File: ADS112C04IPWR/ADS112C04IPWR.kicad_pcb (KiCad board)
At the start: 2 copper layers, 22.9 x 22.9 mm, 3 parts, among them J1 Conn_01x08, J2 Conn_01x08, U1 ADS112C04IPWR

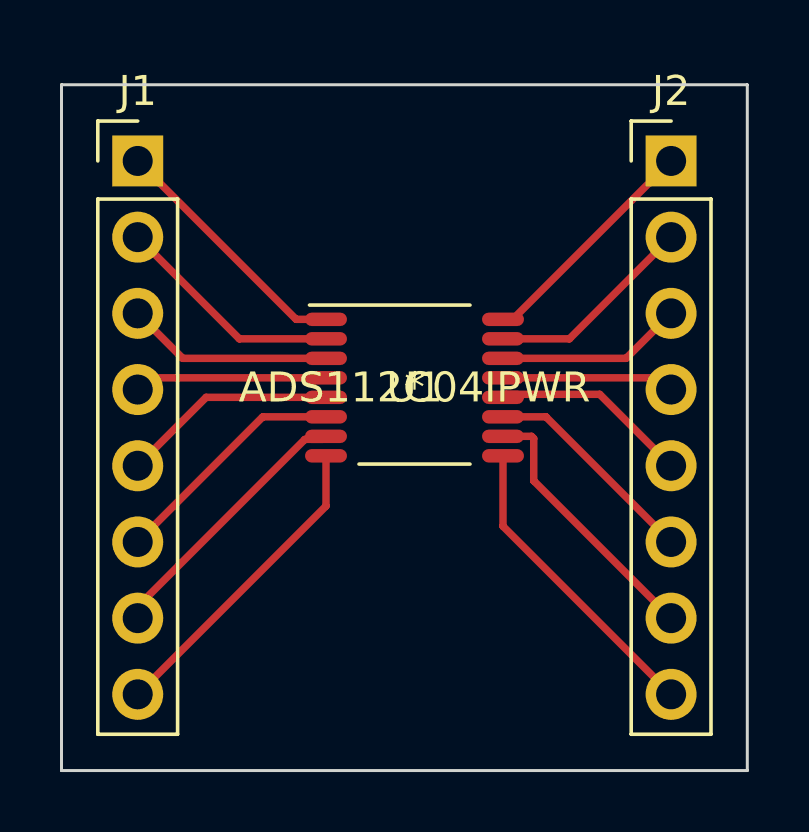
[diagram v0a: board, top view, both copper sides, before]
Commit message: Updating the ADC
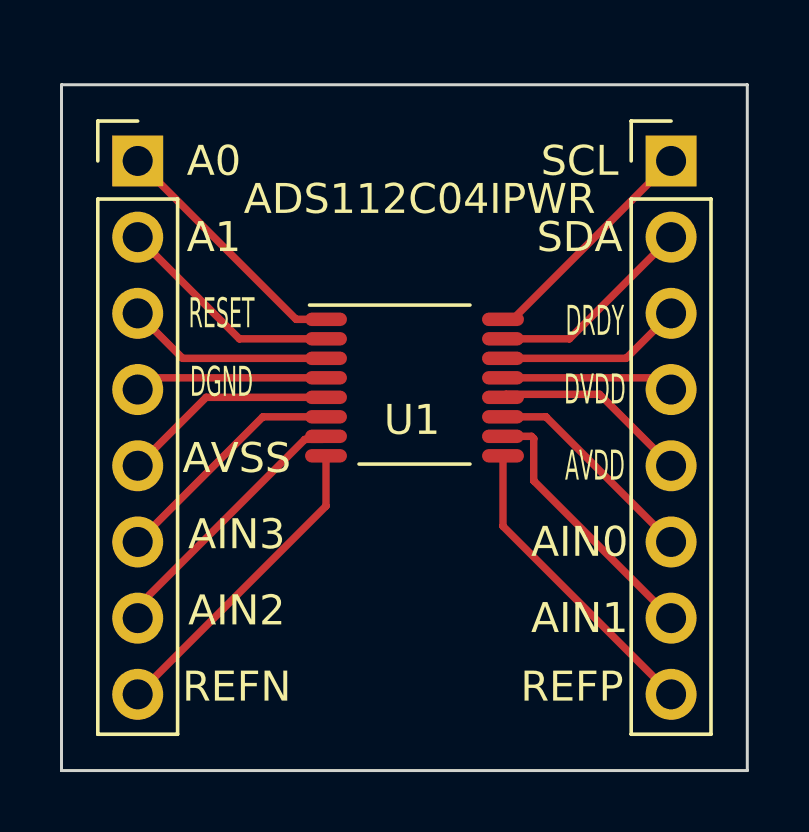
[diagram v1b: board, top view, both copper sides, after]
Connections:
- net Net-(J1-Pad4) renamed GNDD
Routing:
- added copper zone on B.Cu, net GNDD
- added copper zone on F.Cu, net GNDD
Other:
- board text added: "A0"
- board text added: "A1"
- board text added: "AIN0"
- board text added: "AIN1"
- board text added: "AIN2"
- board text added: "AIN3"
- board text added: "AVDD"
- board text added: "AVSS"
- board text added: "DGND"
- board text added: "DRDY"
- board text added: "DVDD"
- board text added: "REFN"
- board text added: "REFP"
- board text added: "RESET"
- board text added: "SCL"
- board text added: "SDA"
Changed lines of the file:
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@@
       (outputformat 1)
       (mirror false)
-      (drillshape 1)
+      (drillshape 0)
       (scaleselection 1)
       (outputdirectory "")
@@
   (net 2 "Net-(J1-Pad2)")
   (net 3 "Net-(J1-Pad3)")
-  (net 4 "Net-(J1-Pad4)")
+  (net 4 "GNDD")
   (net 5 "Net-(J1-Pad5)")
   (net 6 "Net-(J1-Pad6)")
@@
     (property "Sheetfile" "ADS112C04IPWR.kicad_sch")
     (property "Sheetname" "")
-    (attr through_hole)
-    (fp_text reference "U1" (at 0 0) (layer "F.SilkS")
-      (effects (font (size 1 1) (thickness 0.15)))
-    )
-    (fp_text value "ADS112C04IPWR" (at 0 0) (layer "F.SilkS")
-      (effects (font (size 1 1) (thickness 0.15)))
-    )
-    (fp_text user "*" (at 0 0) (layer "F.SilkS")
+    (attr smd)
+    (fp_text reference "U1" (at -0.0826 1.081795) (layer "F.SilkS")
+      (effects (font (size 1 1) (thickness 0.15)))
+    )
+    (fp_text value "ADS112C04IPWR" (at 0.1714 -6.284205) (layer "F.SilkS")
       (effects (font (size 1 1) (thickness 0.15)))
     )
@@
     (fp_line (start -3.9 2.799999) (end -3.9 -2.799999) (layer "F.CrtYd") (width 0.05))
     (fp_line (start 3.9 2.799999) (end 3.9 -2.799999) (layer "F.CrtYd") (width 0.05))
-    (fp_line (start -0.499999 0) (end 0.500002 0) (layer "F.CrtYd") (width 0.05))
     (fp_line (start -3.9 2.799999) (end 3.9 2.799999) (layer "F.CrtYd") (width 0.05))
-    (fp_line (start 0 0.500002) (end 0 -0.499999) (layer "F.CrtYd") (width 0.05))
     (fp_line (start -2.200001 -2.152503) (end -2.200001 -2.397486) (layer "F.Fab") (width 0.1))
     (fp_line (start -2.88669 1.747515) (end -2.739065 1.747515) (layer "F.Fab") (width 0.1))
@@
       (net 3 "Net-(J1-Pad3)") (pinfunction "RESET_N") (pintype "input"))
     (pad "4" smd oval (at -2.949999 -0.324998 90) (size 0.449999 1.4) (layers "F.Cu" "F.Paste" "F.Mask")
-      (net 4 "Net-(J1-Pad4)") (pinfunction "DGND") (pintype "power_in"))
+      (net 4 "GNDD") (pinfunction "DGND") (pintype "power_in"))
     (pad "5" smd oval (at -2.949999 0.325001 90) (size 0.449999 1.4) (layers "F.Cu" "F.Paste" "F.Mask")
       (net 5 "Net-(J1-Pad5)") (pinfunction "AVSS") (pintype "power_in"))
@@
     (property "Sheetname" "")
     (attr through_hole)
-    (fp_text reference "J2" (at 0 -2.33) (layer "F.SilkS")
+    (fp_text reference "J2" (at 0 -2.33) (layer "F.SilkS") hide
       (effects (font (size 1 1) (thickness 0.15)))
     )
@@
     (property "Sheetname" "")
     (attr through_hole)
-    (fp_text reference "J1" (at 0 -2.33) (layer "F.SilkS")
+    (fp_text reference "J1" (at 0 -2.33) (layer "F.SilkS") hide
       (effects (font (size 1 1) (thickness 0.15)))
     )
@@
       (net 3 "Net-(J1-Pad3)") (pinfunction "Pin_3") (pintype "passive"))
     (pad "4" thru_hole oval (at 0 7.62) (size 1.7 1.7) (drill 1) (layers *.Cu *.Mask)
-      (net 4 "Net-(J1-Pad4)") (pinfunction "Pin_4") (pintype "passive"))
+      (net 4 "GNDD") (pinfunction "Pin_4") (pintype "passive"))
     (pad "5" thru_hole oval (at 0 10.16) (size 1.7 1.7) (drill 1) (layers *.Cu *.Mask)
       (net 5 "Net-(J1-Pad5)") (pinfunction "Pin_5") (pintype "passive"))
@@
   )
   (gr_rect (start 142.24 63.5) (end 165.1 86.36) (layer "Edge.Cuts") (width 0.1) (fill none))
+  (gr_text "REFP" (at 159.258 83.566) (layer "F.SilkS")
+    (effects (font (size 1 1) (thickness 0.15)))
+  )
+  (gr_text "AIN1" (at 159.512 81.28) (layer "F.SilkS")
+    (effects (font (size 1 1) (thickness 0.15)))
+  )
+  (gr_text "DGND" (at 147.574 73.406) (layer "F.SilkS")
+    (effects (font (size 1 0.5) (thickness 0.125)))
+  )
+  (gr_text "A1" (at 147.32 68.58) (layer "F.SilkS")
+    (effects (font (size 1 1) (thickness 0.15)))
+  )
+  (gr_text "REFN" (at 148.082 83.566) (layer "F.SilkS")
+    (effects (font (size 1 1) (thickness 0.15)))
+  )
+  (gr_text "AIN2" (at 148.082 81.026) (layer "F.SilkS")
+    (effects (font (size 1 1) (thickness 0.15)))
+  )
+  (gr_text "AVSS" (at 148.082 75.946) (layer "F.SilkS")
+    (effects (font (size 1 1) (thickness 0.15)))
+  )
+  (gr_text "AIN3" (at 148.082 78.486) (layer "F.SilkS")
+    (effects (font (size 1 1) (thickness 0.15)))
+  )
+  (gr_text "AIN0" (at 159.512 78.74) (layer "F.SilkS")
+    (effects (font (size 1 1) (thickness 0.15)))
+  )
+  (gr_text "DVDD" (at 160.02 73.66) (layer "F.SilkS")
+    (effects (font (size 1 0.5) (thickness 0.125)))
+  )
+  (gr_text "RESET" (at 147.574 71.12) (layer "F.SilkS")
+    (effects (font (size 1 0.5) (thickness 0.125)))
+  )
+  (gr_text "DRDY" (at 160.02 71.374) (layer "F.SilkS")
+    (effects (font (size 1 0.5) (thickness 0.125)))
+  )
+  (gr_text "AVDD" (at 160.02 76.2) (layer "F.SilkS")
+    (effects (font (size 1 0.5) (thickness 0.125)))
+  )
+  (gr_text "SCL" (at 159.512 66.04) (layer "F.SilkS")
+    (effects (font (size 1 1) (thickness 0.15)))
+  )
+  (gr_text "SDA" (at 159.512 68.58) (layer "F.SilkS")
+    (effects (font (size 1 1) (thickness 0.15)))
+  )
+  (gr_text "A0" (at 147.32 66.04) (layer "F.SilkS")
+    (effects (font (size 1 1) (thickness 0.15)))
+  )
   (segment (start 144.78 66.04) (end 150.059206 71.319206) (width 0.25) (layer "F.Cu") (net 1))
   (segment (start 150.059206 71.319206) (end 151.056601 71.319206) (width 0.25) (layer "F.Cu") (net 1))
@@
   (segment (start 162.56 83.82) (end 156.956602 78.216602) (width 0.25) (layer "F.Cu") (net 16))
   (segment (start 156.956602 78.216602) (end 156.956602 75.869207) (width 0.25) (layer "F.Cu") (net 16))
+  (zone (net 4) (net_name "GNDD") (layer "F.Cu") (hatch edge 0.508)
+    (connect_pads (clearance 0.508))
+    (min_thickness 0.254) (filled_areas_thickness no)
+    (fill yes (thermal_gap 0.508) (thermal_bridge_width 0.508))
+    (polygon
+      (pts
+        (xy 165.1 86.36)
+        (xy 142.24 86.36)
+        (xy 142.24 63.5)
+        (xy 165.1 63.5)
+      )
+    )
+  )
+  (zone (net 4) (net_name "GNDD") (layer "B.Cu") (hatch edge 0.508)
+    (connect_pads (clearance 0.508))
+    (min_thickness 0.254) (filled_areas_thickness no)
+    (fill yes (thermal_gap 0.508) (thermal_bridge_width 0.508))
+    (polygon
+      (pts
+        (xy 165.1 86.36)
+        (xy 142.24 86.36)
+        (xy 142.24 63.5)
+        (xy 165.1 63.5)
+      )
+    )
+  )
 )

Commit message: Revision One
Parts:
- added C1: 0.1μF, Capacitor_SMD:C_0201_0603Metric_Pad0.64x0.40mm_HandSolder, F.Cu at (149.0, 68.3)
- added C2: 0.1μF, Capacitor_SMD:C_0201_0603Metric_Pad0.64x0.40mm_HandSolder, F.Cu at (148.9, 69.8)
- J1, J2: value Conn_01x08 -> Conn_01x04; footprint Connector_PinHeader_2.54mm:PinHeader_1x08_P2.54mm_Vertical -> Connector_PinHeader_2.54mm:PinHeader_1x04_P2.54mm_Vertical
- moved U1 4.73 mm to (153.9, 68.9), turned to 180 degrees
- moved J1 1.00 mm to (144.1, 65.4)
- moved J2 0.99 mm to (163.3, 65.3)
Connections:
- J1 pad 1: Net-(J1-Pad1) -> /AIN1
- J1 pad 2: Net-(J1-Pad2) -> /AIN0
- J1 pad 3: Net-(J1-Pad3) -> /SDA
- J1 pad 4: GNDD -> /SCL
- J2 pad 1: Net-(J2-Pad1) -> /AIN2
- J2 pad 2: Net-(J2-Pad2) -> /AIN3
- J2 pad 3: Net-(J2-Pad3) -> +3V3
- J2 pad 4: Net-(J2-Pad4) -> GND
- U1 pad 1: Net-(J1-Pad1) -> /SCL
- U1 pad 10: Net-(J2-Pad7) -> /AIN1
- U1 pad 11: Net-(J2-Pad6) -> /AIN0
- U1 pad 12: Net-(J2-Pad5) -> +3V3
- U1 pad 13: Net-(J2-Pad4) -> +3V3
- U1 pad 14: Net-(J2-Pad3) -> unconnected-(U1-Pad14)
- U1 pad 15: Net-(J2-Pad2) -> /SDA
- U1 pad 16: Net-(J2-Pad1) -> /SCL
- U1 pad 2: Net-(J1-Pad2) -> /SCL
- U1 pad 3: Net-(J1-Pad3) -> +3V3
- U1 pad 4: GNDD -> GND
- U1 pad 5: Net-(J1-Pad5) -> GND
- U1 pad 6: Net-(J1-Pad6) -> /AIN3
- U1 pad 7: Net-(J1-Pad7) -> /AIN2
- U1 pad 8: Net-(J1-Pad8) -> unconnected-(U1-Pad8)
- U1 pad 9: Net-(J2-Pad8) -> unconnected-(U1-Pad9)
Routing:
- net +3V3: track 0.00 -> 49.9 mm, vias 0 -> 1
- net /SCL: track 0.00 -> 14.2 mm
- net Net-(J1-Pad8): track 10.6 -> 0.00 mm
- net Net-(J2-Pad8): track 10.3 -> 0.00 mm
- net Net-(J1-Pad7): track 9.01 -> 0.00 mm
- net Net-(J2-Pad7): track 8.94 -> 0.00 mm
- net Net-(J1-Pad1): track 8.46 -> 0.00 mm
- net Net-(J1-Pad6): track 8.00 -> 0.00 mm
- net Net-(J2-Pad1): track 7.79 -> 0.00 mm
- net Net-(J1-Pad2): track 7.68 -> 0.00 mm
- net /AIN1: track 0.00 -> 7.64 mm
- net /SDA: track 0.00 -> 7.48 mm
- net Net-(J2-Pad6): track 7.33 -> 0.00 mm
- net /AIN0: track 0.00 -> 7.33 mm
- net /AIN2: track 0.00 -> 7.24 mm
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- added copper zone on B.Cu, net GND
- added copper zone on F.Cu, net GND
- removed copper zone on B.Cu, net GNDD
- removed copper zone on F.Cu, net GNDD
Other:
- board size 22.9 x 22.9 mm -> 22.9 x 13.2 mm
- board text added: "3v3"
- board text added: "GND"
- board text added: "I²C address 100 1111 (0x4F)"
- board text removed: "A0"
- board text removed: "A1"
- board text removed: "AVDD"
- board text removed: "AVSS"
- board text removed: "DGND"
- board text removed: "DRDY"
- board text removed: "DVDD"
- board text removed: "REFN"
- board text removed: "REFP"
- board text removed: "RESET"
